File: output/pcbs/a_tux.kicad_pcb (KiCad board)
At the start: 2 copper layers, 138.2 x 111.2 mm, 58 parts

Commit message: Added watch scripts, began moving TRRS / pro micro to give myself room
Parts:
- moved REF** 40.3 mm to (114.2, -0.61), turned to -95 degrees
- moved B1 3.00 mm to (112.2, -0.79)
- moved MCU1 3.00 mm to (108.4, -26.2)
- moved _1 3.00 mm to (61.6, -29.8)
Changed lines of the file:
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@@
     )
       (module ProMicro (layer F.Cu)
-      (at 105.3898308 -26.4766647 -95)
+      (at 108.3784149 -26.215197500000002 -95)
       (fp_text reference "MCU1" (at 0 0) (layer F.SilkS) hide (effects (font (size 1.27 1.27) (thickness 0.15))))
       (fp_text value "" (at 0 0) (layer F.SilkS) hide (effects (font (size 1.27 1.27) (thickness 0.15))))
@@
       )
 (module "Tenting Puck" (layer F.Cu)
-  (at 58.624363 -29.7933885 -4)
+  (at 61.624363 -29.7933885 -4)
   (fp_text reference "_1" (at 7.6835 1.4605) (layer F.Fab)
     hide
@@
         (descr "Low-profile SMD Tactile Switch, https://www.e-switch.com/product-catalog/tact/product-lines/tl3342-series-low-profile-smt-tact-switch")
         (tags "SPST Tactile Switch")
-        (at 109.1881054 -1.048862800000002 -95)
+        (at 112.1766895 -0.7873956000000035 -95)
         (fp_text reference "B1" (at 0 0) (layer F.SilkS) hide (effects (font (size 1.27 1.27) (thickness 0.15))))
         (fp_text value "" (at 0 0) (layer F.SilkS) hide (effects (font (size 1.27 1.27) (thickness 0.15))))
@@
     )
       (module TRRS-PJ-320A-dual (layer F.Cu)
-      (at 122.3872334 -40.0468822 -5)
+      (at 114.1690789 -0.6130841000000018 -95)
       (fp_text reference REF** (at 0 14.2) (layer Dwgs.User) (effects (font (size 1 1) (thickness 0.15))))
       (fp_text value TRRS-PJ-320A-dual (at 0 -5.6) (layer F.Fab) (effects (font (size 1 1) (thickness 0.15))))
@@
       (pad "" np_thru_hole circle (at -2.3 8.6) (size 1.5 1.5) (drill 1.5) (layers *.Cu *.Mask))
       (pad "" np_thru_hole circle (at -2.3 1.6) (size 1.5 1.5) (drill 1.5) (layers *.Cu *.Mask))
-        (pad 1 thru_hole oval (at 0 11.3 -5) (size 1.6 2.2) (drill oval 0.9 1.5) (layers *.Cu *.Mask) (net 29 "GND"))
-        (pad 2 thru_hole oval (at -4.6 10.2 -5) (size 1.6 2.2) (drill oval 0.9 1.5) (layers *.Cu *.Mask) (net 29 "GND"))
-        (pad 3 thru_hole oval (at -4.6 6.2 -5) (size 1.6 2.2) (drill oval 0.9 1.5) (layers *.Cu *.Mask) (net 38 "P2"))
-        (pad 4 thru_hole oval (at -4.6 3.2 -5) (size 1.6 2.2) (drill oval 0.9 1.5) (layers *.Cu *.Mask) (net 31 "VCC"))
-        (pad 1 thru_hole oval (at -4.6 11.3 -5) (size 1.6 2.2) (drill oval 0.9 1.5) (layers *.Cu *.Mask) (net 29 "GND"))
-        (pad 2 thru_hole oval (at 0 10.2 -5) (size 1.6 2.2) (drill oval 0.9 1.5) (layers *.Cu *.Mask) (net 29 "GND"))
-        (pad 3 thru_hole oval (at 0 6.2 -5) (size 1.6 2.2) (drill oval 0.9 1.5) (layers *.Cu *.Mask) (net 38 "P2"))
-        (pad 4 thru_hole oval (at 0 3.2 -5) (size 1.6 2.2) (drill oval 0.9 1.5) (layers *.Cu *.Mask) (net 31 "VCC"))
+        (pad 1 thru_hole oval (at 0 11.3 -95) (size 1.6 2.2) (drill oval 0.9 1.5) (layers *.Cu *.Mask) (net 29 "GND"))
+        (pad 2 thru_hole oval (at -4.6 10.2 -95) (size 1.6 2.2) (drill oval 0.9 1.5) (layers *.Cu *.Mask) (net 29 "GND"))
+        (pad 3 thru_hole oval (at -4.6 6.2 -95) (size 1.6 2.2) (drill oval 0.9 1.5) (layers *.Cu *.Mask) (net 38 "P2"))
+        (pad 4 thru_hole oval (at -4.6 3.2 -95) (size 1.6 2.2) (drill oval 0.9 1.5) (layers *.Cu *.Mask) (net 31 "VCC"))
+        (pad 1 thru_hole oval (at -4.6 11.3 -95) (size 1.6 2.2) (drill oval 0.9 1.5) (layers *.Cu *.Mask) (net 29 "GND"))
+        (pad 2 thru_hole oval (at 0 10.2 -95) (size 1.6 2.2) (drill oval 0.9 1.5) (layers *.Cu *.Mask) (net 29 "GND"))
+        (pad 3 thru_hole oval (at 0 6.2 -95) (size 1.6 2.2) (drill oval 0.9 1.5) (layers *.Cu *.Mask) (net 38 "P2"))
+        (pad 4 thru_hole oval (at 0 3.2 -95) (size 1.6 2.2) (drill oval 0.9 1.5) (layers *.Cu *.Mask) (net 31 "VCC"))
       )
             (gr_line (start 7.4949342 12.5678907) (end 24.8815991 7.909147899999999) (angle 90) (layer Edge.Cuts) (width 0.15))

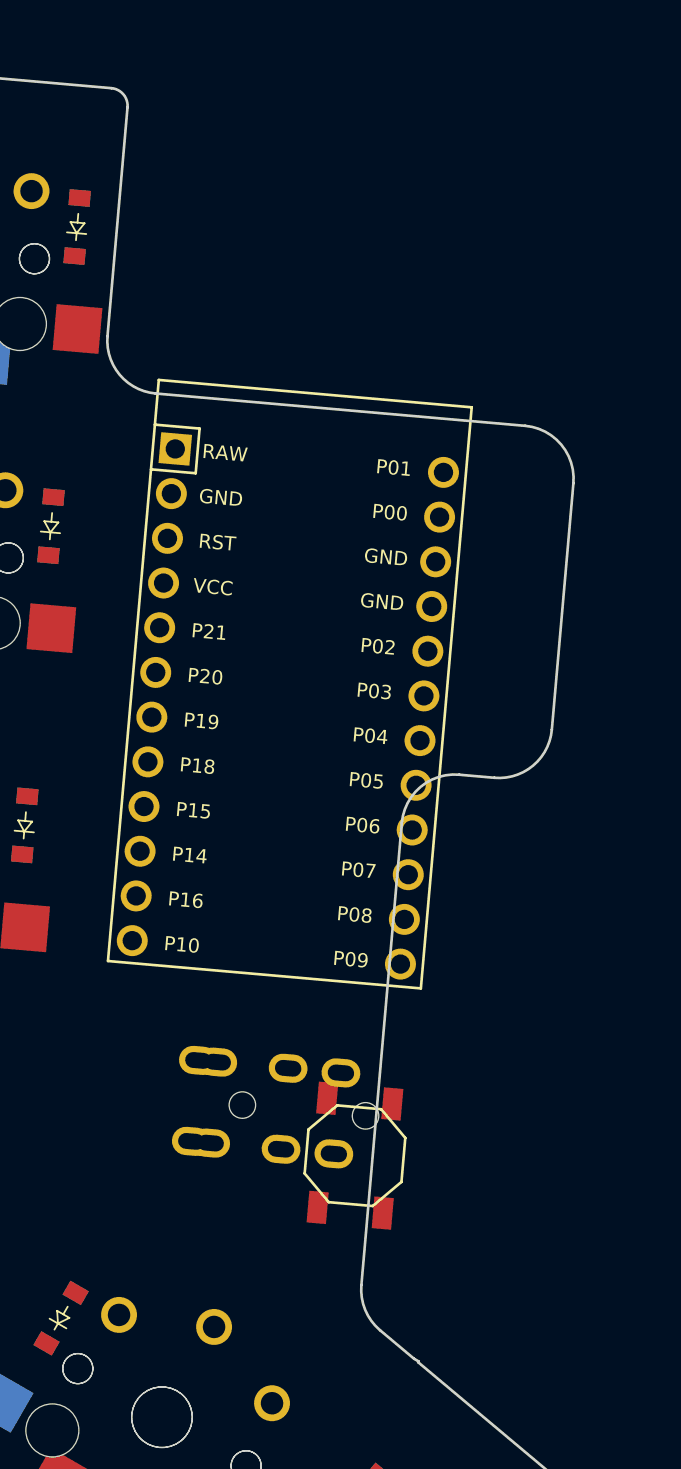
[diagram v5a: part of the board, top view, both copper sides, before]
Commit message: Took care of TRRS problem, widened the pro micro space
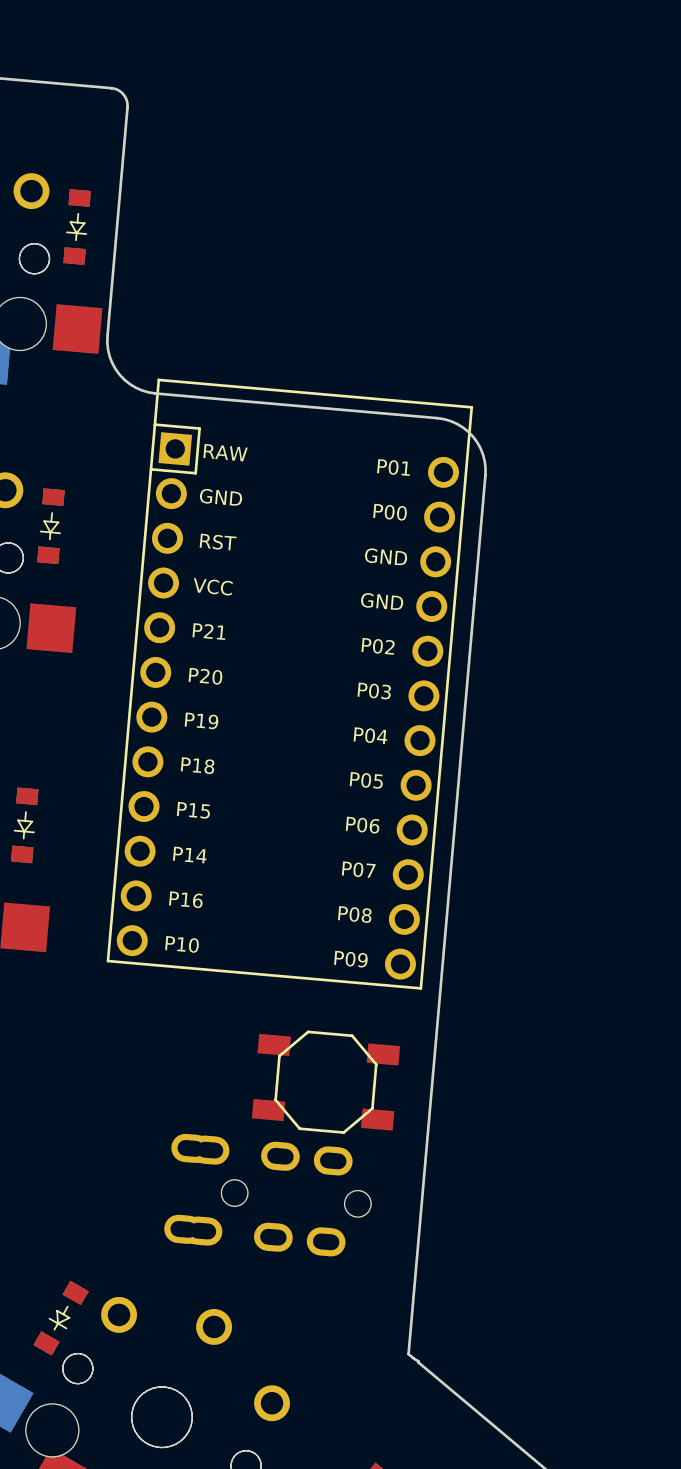
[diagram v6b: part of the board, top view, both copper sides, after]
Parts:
- moved REF** 5.00 mm to (113.7, 4.37)
- moved B1 4.47 mm to (110.5, -4.95), turned to -5 degrees
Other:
- outline, holes or cut-outs redrawn
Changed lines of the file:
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@@
         (descr "Low-profile SMD Tactile Switch, https://www.e-switch.com/product-catalog/tact/product-lines/tl3342-series-low-profile-smt-tact-switch")
         (tags "SPST Tactile Switch")
-        (at 112.1766895 -0.7873956000000035 -95)
+        (at 110.5329231 -4.946485800000001 -5)
         (fp_text reference "B1" (at 0 0) (layer F.SilkS) hide (effects (font (size 1.27 1.27) (thickness 0.15))))
         (fp_text value "" (at 0 0) (layer F.SilkS) hide (effects (font (size 1.27 1.27) (thickness 0.15))))
@@
         (fp_line (start -2.75 -1.25) (end -1.25 -2.75) (layer F.SilkS) (width 0.15))
         (fp_line (start -2.75 -1.25) (end -2.75 1.25) (layer F.SilkS) (width 0.15))
-        (pad 1 smd rect (at -3.1 -1.85 -95) (size 1.8 1.1) (layers F.Cu F.Paste F.Mask) (net 29 "GND"))
-        (pad 1 smd rect (at 3.1 -1.85 -95) (size 1.8 1.1) (layers F.Cu F.Paste F.Mask) (net 29 "GND"))
-        (pad 2 smd rect (at -3.1 1.85 -95) (size 1.8 1.1) (layers F.Cu F.Paste F.Mask) (net 30 "RST"))
-        (pad 2 smd rect (at 3.1 1.85 -95) (size 1.8 1.1) (layers F.Cu F.Paste F.Mask) (net 30 "RST"))
+        (pad 1 smd rect (at -3.1 -1.85 -5) (size 1.8 1.1) (layers F.Cu F.Paste F.Mask) (net 29 "GND"))
+        (pad 1 smd rect (at 3.1 -1.85 -5) (size 1.8 1.1) (layers F.Cu F.Paste F.Mask) (net 29 "GND"))
+        (pad 2 smd rect (at -3.1 1.85 -5) (size 1.8 1.1) (layers F.Cu F.Paste F.Mask) (net 30 "RST"))
+        (pad 2 smd rect (at 3.1 1.85 -5) (size 1.8 1.1) (layers F.Cu F.Paste F.Mask) (net 30 "RST"))
     )
       (module TRRS-PJ-320A-dual (layer F.Cu)
-      (at 114.1690789 -0.6130841000000018 -95)
+      (at 113.7333002 4.367889399999996 -95)
       (fp_text reference REF** (at 0 14.2) (layer Dwgs.User) (effects (font (size 1 1) (thickness 0.15))))
       (fp_text value TRRS-PJ-320A-dual (at 0 -5.6) (layer F.Fab) (effects (font (size 1 1) (thickness 0.15))))
@@
 (gr_arc (start 80.6194601 -64.614002) (end 81.6156548 -64.5268463) (angle -90) (layer Edge.Cuts) (width 0.15))
 (gr_line (start 61.3628959992404 -67.30255292146246) (end 80.70661580000001 -65.61019669999999) (angle 90) (layer Edge.Cuts) (width 0.15))
-(gr_line (start 112.53981412016309 6.535784695219718) (end 114.82884329845986 -19.627938915982895) (angle 90) (layer Edge.Cuts) (width 0.15))
-(gr_line (start 100.89431023321649 -43.93490902566536) (end 121.81439876850617 -42.104638440075654) (angle 90) (layer Edge.Cuts) (width 0.15))
-(gr_line (start 123.32133534597864 -24.907861425486317) (end 124.54151577642897 -38.85458723063357) (angle 90) (layer Edge.Cuts) (width 0.15))
-(gr_line (start 120.07128413653662 -22.180744417563403) (end 118.07889450790185 -22.355055923905557) (angle 90) (layer Edge.Cuts) (width 0.15))
-(gr_line (start 98.16719322529373 -47.18496023510761) (end 99.3002179 -60.1354913) (angle 90) (layer Edge.Cuts) (width 0.15))
+(gr_line (start 115.2092056930235 10.445639281275135) (end 118.77614059999999 -30.3246134) (angle 90) (layer Edge.Cuts) (width 0.15))
+(gr_line (start 100.89431023300081 -43.93490902319976) (end 116.8334252537819 -42.54041714322722) (angle 90) (layer Edge.Cuts) (width 0.15))
+(gr_line (start 119.56054226170468 -39.2903659337851) (end 118.950452 -32.317002900000006) (angle 90) (layer Edge.Cuts) (width 0.15))
+(gr_line (start 118.950452 -32.317002900000006) (end 118.77614059999999 -30.3246134) (angle 90) (layer Edge.Cuts) (width 0.15))
+(gr_line (start 98.16719322507801 -47.18496023264174) (end 99.3002179 -60.1354913) (angle 90) (layer Edge.Cuts) (width 0.15))
 (gr_arc (start 98.30402320000002 -60.222647) (end 99.30021790000002 -60.135491300000005) (angle -90) (layer Edge.Cuts) (width 0.15))
 (gr_line (start 81.45586924858333 -62.700489333807326) (end 98.3911789 -61.2188417) (angle 90) (layer Edge.Cuts) (width 0.15))
 (gr_line (start 27.62467391536008 -3.9567581825079525) (end 88.24812504522723 18.108373547250363) (angle 90) (layer Edge.Cuts) (width 0.15))
 (gr_line (start 88.72206470139008 18.329375267691972) (end 103.78015051367868 27.023165202888215) (angle 90) (layer Edge.Cuts) (width 0.15))
-(gr_line (start 115.52280078985663 10.708776813339554) (end 115.7773866 10.855762) (angle 90) (layer Edge.Cuts) (width 0.15))
+(gr_line (start 115.52280078985667 10.708776813339583) (end 115.7773866 10.855762) (angle 90) (layer Edge.Cuts) (width 0.15))
 (gr_line (start 115.7773866 10.855762) (end 115.75146914555461 10.900652347706085) (angle 90) (layer Edge.Cuts) (width 0.15))
 (gr_line (start 104.20851336291909 27.32310814420582) (end 117.76274199999999 38.6964564) (angle 90) (layer Edge.Cuts) (width 0.15))
@@
 (gr_arc (start 129.9757066 24.141612) (end 130.741751 24.784399599999997) (angle -90) (layer Edge.Cuts) (width 0.15))
 (gr_line (start 115.75146914555461 10.9006523477061) (end 130.6184942 23.375567599999997) (angle 90) (layer Edge.Cuts) (width 0.15))
-(gr_line (start 113.60003537960509 9.095385054661705) (end 115.52280078985663 10.708776813339554) (angle 90) (layer Edge.Cuts) (width 0.15))
+(gr_line (start 115.2092056930235 10.445639281275163) (end 115.52280078985667 10.708776813339583) (angle 90) (layer Edge.Cuts) (width 0.15))
 (gr_arc (start 26.59861357152293 -1.137680262066354) (end 27.62467387152293 -3.956758162066354) (angle -124.9999959683712) (layer Edge.Cuts) (width 0.15))
 (gr_arc (start 87.22206470139008 20.927451467691974) (end 88.72206470139008 18.329375267691972) (angle -10.000002033761568) (layer Edge.Cuts) (width 0.15))
 (gr_arc (start 102.28015051367869 29.621241402888224) (end 104.20851341367869 27.323108102888224) (angle -10.000001054460988) (layer Edge.Cuts) (width 0.15))
-(gr_arc (start 115.52839822884549 6.797251795979292) (end 112.53981412884549 6.5357846959792925) (angle -54.99999638765314) (layer Edge.Cuts) (width 0.15))
-(gr_arc (start 117.81742740714225 -19.36647181522312) (end 118.07889450714225 -22.355055915223122) (angle -89.99999999999667) (layer Edge.Cuts) (width 0.15))
-(gr_arc (start 120.33275123729622 -25.169328526245813) (end 120.07128413729622 -22.180744426245813) (angle -90.0000000000021) (layer Edge.Cuts) (width 0.15))
-(gr_arc (start 121.55293166774655 -39.116054331393116) (end 124.54151576774655 -38.85458723139312) (angle -89.99999999999888) (layer Edge.Cuts) (width 0.15))
-(gr_arc (start 101.15577733397612 -46.92349313434777) (end 98.16719323397612 -47.18496023434777) (angle -90.00000000000398) (layer Edge.Cuts) (width 0.15))
+(gr_arc (start 116.57195815302228 -39.55183303454464) (end 119.56054225302228 -39.290365934544646) (angle -89.99999999999893) (layer Edge.Cuts) (width 0.15))
+(gr_arc (start 101.15577733376041 -46.92349313188217) (end 98.16719323376041 -47.184960231882165) (angle -89.99999999999946) (layer Edge.Cuts) (width 0.15))
 (gr_arc (start 61.624363100000004 -70.29113703014487) (end 58.624363100000004 -70.29113703014487) (angle -85.00000244946955) (layer Edge.Cuts) (width 0.15))
 (gr_arc (start 35.624363100000004 -68.72969085435393) (end 35.8858302 -65.74110675435394) (angle -85.00000244946955) (layer Edge.Cuts) (width 0.15))

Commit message: Removed reversible pro micro footprint, seems impossible to actually route
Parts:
- added T1: , E73:SPDT_C128955, F.Cu at (114.6, -5.59)
- turned B1 to 175 degrees
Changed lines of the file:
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@@
 (net 39 "P3")
 (net 40 "P4")
+(net 41 "P01")
   (net_class Default "This is the default net class."
     (clearance 0.2)
@@
 (add_net "P3")
 (add_net "P4")
+(add_net "P01")
   )
       (module PG1350 (layer F.Cu)
@@
         (descr "Low-profile SMD Tactile Switch, https://www.e-switch.com/product-catalog/tact/product-lines/tl3342-series-low-profile-smt-tact-switch")
         (tags "SPST Tactile Switch")
-        (at 110.5329231 -4.946485800000001 -5)
+        (at 110.5329231 -4.946485800000001 175)
         (fp_text reference "B1" (at 0 0) (layer F.SilkS) hide (effects (font (size 1.27 1.27) (thickness 0.15))))
         (fp_text value "" (at 0 0) (layer F.SilkS) hide (effects (font (size 1.27 1.27) (thickness 0.15))))
@@
         (fp_line (start -2.75 -1.25) (end -1.25 -2.75) (layer F.SilkS) (width 0.15))
         (fp_line (start -2.75 -1.25) (end -2.75 1.25) (layer F.SilkS) (width 0.15))
-        (pad 1 smd rect (at -3.1 -1.85 -5) (size 1.8 1.1) (layers F.Cu F.Paste F.Mask) (net 29 "GND"))
-        (pad 1 smd rect (at 3.1 -1.85 -5) (size 1.8 1.1) (layers F.Cu F.Paste F.Mask) (net 29 "GND"))
-        (pad 2 smd rect (at -3.1 1.85 -5) (size 1.8 1.1) (layers F.Cu F.Paste F.Mask) (net 30 "RST"))
-        (pad 2 smd rect (at 3.1 1.85 -5) (size 1.8 1.1) (layers F.Cu F.Paste F.Mask) (net 30 "RST"))
+        (pad 1 smd rect (at -3.1 -1.85 175) (size 1.8 1.1) (layers F.Cu F.Paste F.Mask) (net 29 "GND"))
+        (pad 1 smd rect (at 3.1 -1.85 175) (size 1.8 1.1) (layers F.Cu F.Paste F.Mask) (net 29 "GND"))
+        (pad 2 smd rect (at -3.1 1.85 175) (size 1.8 1.1) (layers F.Cu F.Paste F.Mask) (net 30 "RST"))
+        (pad 2 smd rect (at 3.1 1.85 175) (size 1.8 1.1) (layers F.Cu F.Paste F.Mask) (net 30 "RST"))
     )
       (module TRRS-PJ-320A-dual (layer F.Cu)
@@
         (pad 4 thru_hole oval (at 0 3.2 -95) (size 1.6 2.2) (drill oval 0.9 1.5) (layers *.Cu *.Mask) (net 31 "VCC"))
       )
+        (module E73:SPDT_C128955 (layer F.Cu)
+            (at 114.6048576 -5.594057600000003 -95)
+            (fp_text reference "T1" (at 0 0) (layer F.SilkS) hide (effects (font (size 1.27 1.27) (thickness 0.15))))
+            (fp_text value "" (at 0 0) (layer F.SilkS) hide (effects (font (size 1.27 1.27) (thickness 0.15))))
+            (fp_line (start 1.95 -1.35) (end -1.95 -1.35) (layer F.SilkS) (width 0.15))
+            (fp_line (start 0 -1.35) (end -3.3 -1.35) (layer F.SilkS) (width 0.15))
+            (fp_line (start -3.3 -1.35) (end -3.3 1.5) (layer F.SilkS) (width 0.15))
+            (fp_line (start -3.3 1.5) (end 3.3 1.5) (layer F.SilkS) (width 0.15))
+            (fp_line (start 3.3 1.5) (end 3.3 -1.35) (layer F.SilkS) (width 0.15))
+            (fp_line (start 0 -1.35) (end 3.3 -1.35) (layer F.SilkS) (width 0.15))
+            (fp_line (start -1.95 -3.85) (end 1.95 -3.85) (layer Dwgs.User) (width 0.15))
+            (fp_line (start 1.95 -3.85) (end 1.95 -1.35) (layer Dwgs.User) (width 0.15))
+            (fp_line (start -1.95 -1.35) (end -1.95 -3.85) (layer Dwgs.User) (width 0.15))
+            (pad "" np_thru_hole circle (at 1.5 0) (size 1 1) (drill 0.9) (layers *.Cu *.Mask))
+            (pad "" np_thru_hole circle (at -1.5 0) (size 1 1) (drill 0.9) (layers *.Cu *.Mask))
+            (pad 1 smd rect (at 2.25 2.075 -95) (size 0.9 1.25) (layers F.Cu F.Paste F.Mask) (net 29 "GND"))
+            (pad 2 smd rect (at -0.75 2.075 -95) (size 0.9 1.25) (layers F.Cu F.Paste F.Mask) (net 41 "P01"))
+            (pad 3 smd rect (at -2.25 2.075 -95) (size 0.9 1.25) (layers F.Cu F.Paste F.Mask))
+            (pad "" smd rect (at 3.7 -1.1 -95) (size 0.9 0.9) (layers F.Cu F.Paste F.Mask))
+            (pad "" smd rect (at 3.7 1.1 -95) (size 0.9 0.9) (layers F.Cu F.Paste F.Mask))
+            (pad "" smd rect (at -3.7 1.1 -95) (size 0.9 0.9) (layers F.Cu F.Paste F.Mask))
+            (pad "" smd rect (at -3.7 -1.1 -95) (size 0.9 0.9) (layers F.Cu F.Paste F.Mask))
+        )
             (gr_line (start 7.4949342 12.5678907) (end 24.8815991 7.909147899999999) (angle 90) (layer Edge.Cuts) (width 0.15))
 (gr_arc (start 24.622780000000002 6.943221999999999) (end 24.881599 7.909147799999999) (angle -90) (layer Edge.Cuts) (width 0.15))
